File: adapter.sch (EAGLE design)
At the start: 3 parts

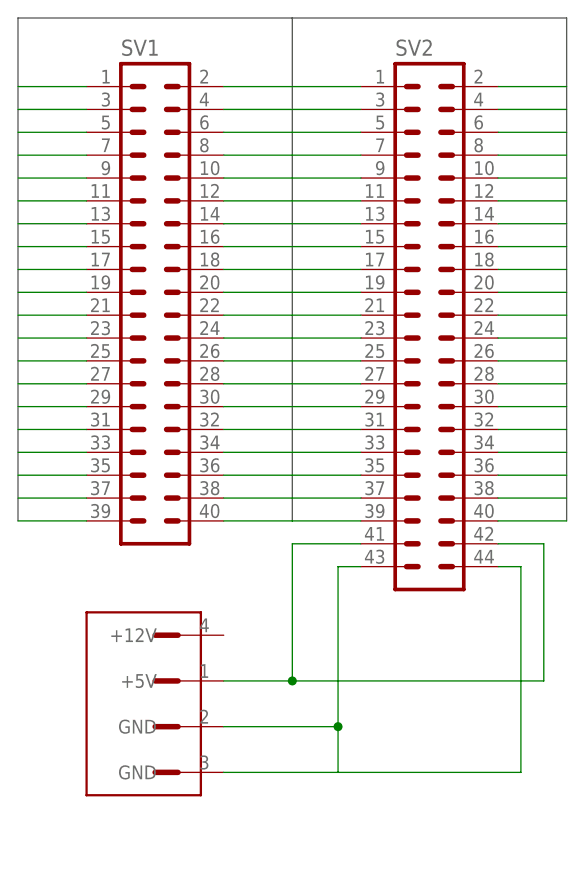
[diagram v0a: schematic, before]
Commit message: Connected the ground together.
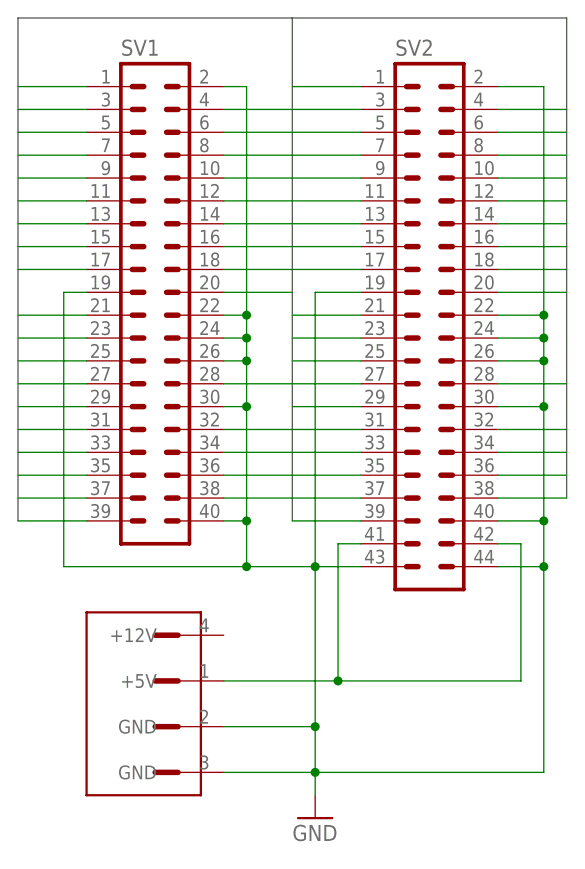
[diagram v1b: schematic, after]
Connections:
- removed net IDE19: SV1.GND@1, SV2.GND@1
- removed net IDE2: SV1.GND@2, SV2.GND@2
- removed net IDE22: SV1.GND@3, SV2.GND@3
- removed net IDE24: SV1.GND@4, SV2.GND@4
- removed net IDE26: SV1.GND@5, SV2.GND@5
- removed net IDE30: SV1.GND@6, SV2.GND@6
- removed net IDE40: SV1.GND@7, SV2.GND@7
- removed net N$1: SV2.!TYPE!, SV2.GND@8, U$1.GND@1, U$1.GND@2
- new net GND: SV1.GND@1, SV1.GND@2, SV1.GND@3, SV1.GND@4, SV1.GND@5, SV1.GND@6, SV1.GND@7, SV2.!TYPE!, SV2.GND@1, SV2.GND@2, SV2.GND@3, SV2.GND@4, SV2.GND@5, SV2.GND@6, SV2.GND@7, SV2.GND@8, U$1.GND@1, U$1.GND@2
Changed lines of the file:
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@@
 <part name="SV2" library="conn" deviceset="IDE44" device="F"/>
 <part name="U$1" library="conn" deviceset="FLOPPYPWR" device=""/>
+<part name="GND1" library="supply1" deviceset="GND" device=""/>
 </parts>
 <sheets>
@@
 <instance part="SV2" gate="1" x="71.12" y="35.56"/>
 <instance part="U$1" gate="G$1" x="40.64" y="-7.62"/>
+<instance part="GND1" gate="1" x="58.42" y="-20.32"/>
 </instances>
 <busses>
@@
 <wire x1="55.88" y1="12.7" x2="55.88" y2="68.58" width="0.762" layer="92"/>
 <wire x1="55.88" y1="68.58" x2="86.36" y2="68.58" width="0.762" layer="92"/>
-<wire x1="86.36" y1="68.58" x2="86.36" y2="12.7" width="0.762" layer="92"/>
+<wire x1="86.36" y1="68.58" x2="86.36" y2="15.24" width="0.762" layer="92"/>
 <wire x1="55.88" y1="68.58" x2="25.4" y2="68.58" width="0.762" layer="92"/>
 <wire x1="25.4" y1="68.58" x2="25.4" y2="12.7" width="0.762" layer="92"/>
@@
 </segment>
 </net>
-<net name="IDE19" class="0">
-<segment>
-<pinref part="SV1" gate="1" pin="GND@1"/>
-<wire x1="33.02" y1="38.1" x2="25.4" y2="38.1" width="0.1524" layer="91"/>
-</segment>
-<segment>
-<pinref part="SV2" gate="1" pin="GND@1"/>
-<wire x1="63.5" y1="38.1" x2="55.88" y2="38.1" width="0.1524" layer="91"/>
-</segment>
-</net>
 <net name="IDE21" class="0">
 <segment>
@@
 </segment>
 </net>
-<net name="IDE2" class="0">
-<segment>
+<net name="GND" class="0">
+<segment>
+<pinref part="U$1" gate="G$1" pin="GND@2"/>
+<wire x1="48.26" y1="-15.24" x2="58.42" y2="-15.24" width="0.1524" layer="91"/>
+<wire x1="58.42" y1="-15.24" x2="58.42" y2="-10.16" width="0.1524" layer="91"/>
+<pinref part="SV2" gate="1" pin="GND@8"/>
+<wire x1="58.42" y1="-10.16" x2="58.42" y2="7.62" width="0.1524" layer="91"/>
+<wire x1="58.42" y1="7.62" x2="63.5" y2="7.62" width="0.1524" layer="91"/>
+<pinref part="U$1" gate="G$1" pin="GND@1"/>
+<wire x1="48.26" y1="-10.16" x2="58.42" y2="-10.16" width="0.1524" layer="91"/>
+<junction x="58.42" y="-10.16"/>
+<pinref part="SV2" gate="1" pin="!TYPE!"/>
+<wire x1="78.74" y1="7.62" x2="83.82" y2="7.62" width="0.1524" layer="91"/>
+<wire x1="83.82" y1="7.62" x2="83.82" y2="-15.24" width="0.1524" layer="91"/>
+<wire x1="83.82" y1="-15.24" x2="58.42" y2="-15.24" width="0.1524" layer="91"/>
+<pinref part="GND1" gate="1" pin="GND"/>
+<wire x1="58.42" y1="-15.24" x2="58.42" y2="-17.78" width="0.1524" layer="91"/>
+<junction x="58.42" y="-15.24"/>
+<pinref part="SV2" gate="1" pin="GND@2"/>
+<wire x1="78.74" y1="60.96" x2="83.82" y2="60.96" width="0.1524" layer="91"/>
+<wire x1="83.82" y1="60.96" x2="83.82" y2="35.56" width="0.1524" layer="91"/>
+<pinref part="SV2" gate="1" pin="GND@5"/>
+<wire x1="83.82" y1="35.56" x2="83.82" y2="33.02" width="0.1524" layer="91"/>
+<wire x1="83.82" y1="33.02" x2="83.82" y2="30.48" width="0.1524" layer="91"/>
+<wire x1="83.82" y1="30.48" x2="83.82" y2="25.4" width="0.1524" layer="91"/>
+<wire x1="83.82" y1="25.4" x2="83.82" y2="12.7" width="0.1524" layer="91"/>
+<wire x1="83.82" y1="12.7" x2="83.82" y2="7.62" width="0.1524" layer="91"/>
+<wire x1="78.74" y1="30.48" x2="83.82" y2="30.48" width="0.1524" layer="91"/>
+<pinref part="SV2" gate="1" pin="GND@4"/>
+<wire x1="78.74" y1="33.02" x2="83.82" y2="33.02" width="0.1524" layer="91"/>
+<pinref part="SV2" gate="1" pin="GND@3"/>
+<wire x1="78.74" y1="35.56" x2="83.82" y2="35.56" width="0.1524" layer="91"/>
+<pinref part="SV2" gate="1" pin="GND@1"/>
+<wire x1="63.5" y1="38.1" x2="58.42" y2="38.1" width="0.1524" layer="91"/>
+<wire x1="58.42" y1="38.1" x2="58.42" y2="7.62" width="0.1524" layer="91"/>
+<junction x="58.42" y="7.62"/>
+<junction x="83.82" y="7.62"/>
+<junction x="83.82" y="30.48"/>
+<junction x="83.82" y="33.02"/>
+<junction x="83.82" y="35.56"/>
+<pinref part="SV2" gate="1" pin="GND@6"/>
+<wire x1="83.82" y1="25.4" x2="78.74" y2="25.4" width="0.1524" layer="91"/>
+<junction x="83.82" y="25.4"/>
+<pinref part="SV2" gate="1" pin="GND@7"/>
+<wire x1="78.74" y1="12.7" x2="83.82" y2="12.7" width="0.1524" layer="91"/>
+<junction x="83.82" y="12.7"/>
+<pinref part="SV1" gate="1" pin="GND@3"/>
+<wire x1="48.26" y1="35.56" x2="50.8" y2="35.56" width="0.1524" layer="91"/>
+<wire x1="50.8" y1="35.56" x2="50.8" y2="33.02" width="0.1524" layer="91"/>
+<wire x1="50.8" y1="33.02" x2="50.8" y2="30.48" width="0.1524" layer="91"/>
+<wire x1="50.8" y1="30.48" x2="50.8" y2="25.4" width="0.1524" layer="91"/>
+<wire x1="50.8" y1="25.4" x2="50.8" y2="12.7" width="0.1524" layer="91"/>
+<wire x1="50.8" y1="12.7" x2="50.8" y2="7.62" width="0.1524" layer="91"/>
+<wire x1="50.8" y1="7.62" x2="58.42" y2="7.62" width="0.1524" layer="91"/>
+<pinref part="SV1" gate="1" pin="GND@7"/>
+<wire x1="48.26" y1="12.7" x2="50.8" y2="12.7" width="0.1524" layer="91"/>
+<pinref part="SV1" gate="1" pin="GND@6"/>
+<wire x1="48.26" y1="25.4" x2="50.8" y2="25.4" width="0.1524" layer="91"/>
+<pinref part="SV1" gate="1" pin="GND@4"/>
+<wire x1="48.26" y1="33.02" x2="50.8" y2="33.02" width="0.1524" layer="91"/>
+<pinref part="SV1" gate="1" pin="GND@5"/>
+<wire x1="48.26" y1="30.48" x2="50.8" y2="30.48" width="0.1524" layer="91"/>
 <pinref part="SV1" gate="1" pin="GND@2"/>
-<wire x1="48.26" y1="60.96" x2="55.88" y2="60.96" width="0.1524" layer="91"/>
-</segment>
-<segment>
-<pinref part="SV2" gate="1" pin="GND@2"/>
-<wire x1="78.74" y1="60.96" x2="86.36" y2="60.96" width="0.1524" layer="91"/>
+<wire x1="48.26" y1="60.96" x2="50.8" y2="60.96" width="0.1524" layer="91"/>
+<wire x1="50.8" y1="60.96" x2="50.8" y2="35.56" width="0.1524" layer="91"/>
+<pinref part="SV1" gate="1" pin="GND@1"/>
+<wire x1="33.02" y1="38.1" x2="30.48" y2="38.1" width="0.1524" layer="91"/>
+<wire x1="30.48" y1="38.1" x2="30.48" y2="7.62" width="0.1524" layer="91"/>
+<wire x1="30.48" y1="7.62" x2="50.8" y2="7.62" width="0.1524" layer="91"/>
+<junction x="50.8" y="35.56"/>
+<junction x="50.8" y="33.02"/>
+<junction x="50.8" y="30.48"/>
+<junction x="50.8" y="25.4"/>
+<junction x="50.8" y="12.7"/>
+<junction x="50.8" y="7.62"/>
 </segment>
 </net>
@@
 </segment>
 </net>
-<net name="IDE22" class="0">
-<segment>
-<pinref part="SV1" gate="1" pin="GND@3"/>
-<wire x1="48.26" y1="35.56" x2="55.88" y2="35.56" width="0.1524" layer="91"/>
-</segment>
-<segment>
-<pinref part="SV2" gate="1" pin="GND@3"/>
-<wire x1="78.74" y1="35.56" x2="86.36" y2="35.56" width="0.1524" layer="91"/>
-</segment>
-</net>
-<net name="IDE24" class="0">
-<segment>
-<pinref part="SV1" gate="1" pin="GND@4"/>
-<wire x1="48.26" y1="33.02" x2="55.88" y2="33.02" width="0.1524" layer="91"/>
-</segment>
-<segment>
-<pinref part="SV2" gate="1" pin="GND@4"/>
-<wire x1="78.74" y1="33.02" x2="86.36" y2="33.02" width="0.1524" layer="91"/>
-</segment>
-</net>
-<net name="IDE26" class="0">
-<segment>
-<pinref part="SV1" gate="1" pin="GND@5"/>
-<wire x1="48.26" y1="30.48" x2="55.88" y2="30.48" width="0.1524" layer="91"/>
-</segment>
-<segment>
-<pinref part="SV2" gate="1" pin="GND@5"/>
-<wire x1="78.74" y1="30.48" x2="86.36" y2="30.48" width="0.1524" layer="91"/>
-</segment>
-</net>
 <net name="IDE28" class="0">
 <segment>
@@
 </segment>
 </net>
-<net name="IDE30" class="0">
-<segment>
-<pinref part="SV1" gate="1" pin="GND@6"/>
-<wire x1="48.26" y1="25.4" x2="55.88" y2="25.4" width="0.1524" layer="91"/>
-</segment>
-<segment>
-<pinref part="SV2" gate="1" pin="GND@6"/>
-<wire x1="78.74" y1="25.4" x2="86.36" y2="25.4" width="0.1524" layer="91"/>
-</segment>
-</net>
 <net name="IDE32" class="0">
 <segment>
@@
 </segment>
 </net>
-<net name="IDE40" class="0">
-<segment>
-<pinref part="SV1" gate="1" pin="GND@7"/>
-<wire x1="48.26" y1="12.7" x2="55.88" y2="12.7" width="0.1524" layer="91"/>
-</segment>
-<segment>
-<pinref part="SV2" gate="1" pin="GND@7"/>
-<wire x1="78.74" y1="12.7" x2="86.36" y2="12.7" width="0.1524" layer="91"/>
-</segment>
-</net>
-<net name="N$1" class="0">
-<segment>
-<pinref part="U$1" gate="G$1" pin="GND@2"/>
-<wire x1="48.26" y1="-15.24" x2="60.96" y2="-15.24" width="0.1524" layer="91"/>
-<wire x1="60.96" y1="-15.24" x2="60.96" y2="-10.16" width="0.1524" layer="91"/>
-<pinref part="SV2" gate="1" pin="GND@8"/>
-<wire x1="60.96" y1="-10.16" x2="60.96" y2="7.62" width="0.1524" layer="91"/>
-<wire x1="60.96" y1="7.62" x2="63.5" y2="7.62" width="0.1524" layer="91"/>
-<pinref part="U$1" gate="G$1" pin="GND@1"/>
-<wire x1="48.26" y1="-10.16" x2="60.96" y2="-10.16" width="0.1524" layer="91"/>
-<junction x="60.96" y="-10.16"/>
-<pinref part="SV2" gate="1" pin="!TYPE!"/>
-<wire x1="78.74" y1="7.62" x2="81.28" y2="7.62" width="0.1524" layer="91"/>
-<wire x1="81.28" y1="7.62" x2="81.28" y2="-15.24" width="0.1524" layer="91"/>
-<wire x1="81.28" y1="-15.24" x2="60.96" y2="-15.24" width="0.1524" layer="91"/>
-</segment>
-</net>
 <net name="N$3" class="0">
 <segment>
 <pinref part="U$1" gate="G$1" pin="+5V"/>
-<wire x1="48.26" y1="-5.08" x2="55.88" y2="-5.08" width="0.1524" layer="91"/>
-<wire x1="55.88" y1="-5.08" x2="55.88" y2="10.16" width="0.1524" layer="91"/>
+<wire x1="48.26" y1="-5.08" x2="60.96" y2="-5.08" width="0.1524" layer="91"/>
+<wire x1="60.96" y1="-5.08" x2="81.28" y2="-5.08" width="0.1524" layer="91"/>
+<wire x1="81.28" y1="-5.08" x2="81.28" y2="10.16" width="0.1524" layer="91"/>
+<pinref part="SV2" gate="1" pin="VCC@2"/>
+<wire x1="81.28" y1="10.16" x2="78.74" y2="10.16" width="0.1524" layer="91"/>
 <pinref part="SV2" gate="1" pin="VCC@1"/>
-<wire x1="55.88" y1="10.16" x2="63.5" y2="10.16" width="0.1524" layer="91"/>
-<wire x1="55.88" y1="-5.08" x2="83.82" y2="-5.08" width="0.1524" layer="91"/>
-<wire x1="83.82" y1="-5.08" x2="83.82" y2="10.16" width="0.1524" layer="91"/>
-<pinref part="SV2" gate="1" pin="VCC@2"/>
-<wire x1="83.82" y1="10.16" x2="78.74" y2="10.16" width="0.1524" layer="91"/>
-<junction x="55.88" y="-5.08"/>
-</segment>
-</net>
+<wire x1="63.5" y1="10.16" x2="60.96" y2="10.16" width="0.1524" layer="91"/>
+<wire x1="60.96" y1="10.16" x2="60.96" y2="-5.08" width="0.1524" layer="91"/>
+<junction x="60.96" y="-5.08"/>
+</segment>
+</net>

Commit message: Reduced pin pitch on the IDE 44 connector.
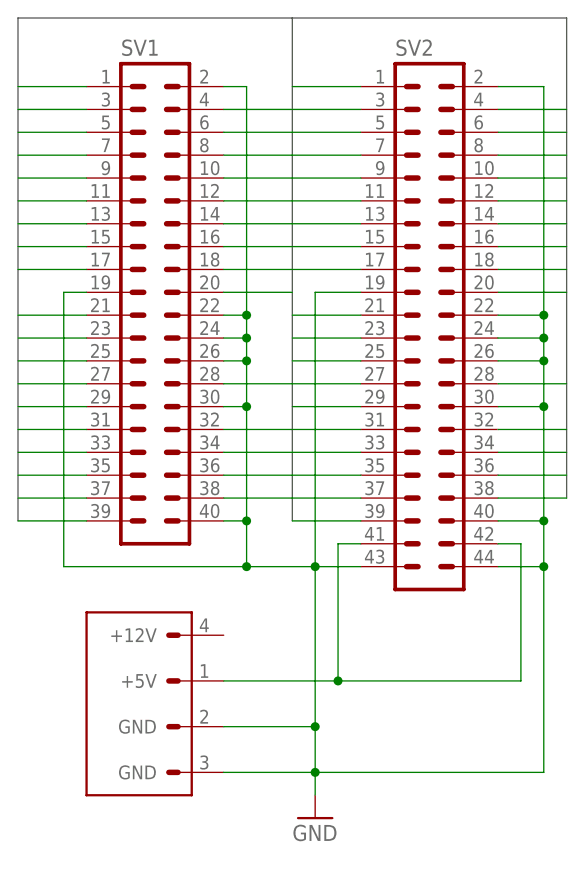
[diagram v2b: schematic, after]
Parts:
- SV2: device conn:IDE44F -> conn:IDE44LOWPITCHF
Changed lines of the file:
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@@
 <grid distance="0.1" unitdist="inch" unit="inch" style="lines" multiple="1" display="no" altdistance="0.01" altunitdist="inch" altunit="inch"/>
 <layers>
-<layer number="1" name="Top" color="4" fill="1" visible="no" active="no"/>
-<layer number="16" name="Bottom" color="1" fill="1" visible="no" active="no"/>
-<layer number="17" name="Pads" color="2" fill="1" visible="no" active="no"/>
-<layer number="18" name="Vias" color="2" fill="1" visible="no" active="no"/>
-<layer number="19" name="Unrouted" color="6" fill="1" visible="no" active="no"/>
-<layer number="20" name="Dimension" color="15" fill="1" visible="no" active="no"/>
-<layer number="21" name="tPlace" color="7" fill="1" visible="no" active="no"/>
-<layer number="22" name="bPlace" color="7" fill="1" visible="no" active="no"/>
-<layer number="23" name="tOrigins" color="15" fill="1" visible="no" active="no"/>
-<layer number="24" name="bOrigins" color="15" fill="1" visible="no" active="no"/>
-<layer number="25" name="tNames" color="7" fill="1" visible="no" active="no"/>
-<layer number="26" name="bNames" color="7" fill="1" visible="no" active="no"/>
-<layer number="27" name="tValues" color="7" fill="1" visible="no" active="no"/>
-<layer number="28" name="bValues" color="7" fill="1" visible="no" active="no"/>
+<layer number="1" name="Top" color="4" fill="1" visible="yes" active="no"/>
+<layer number="16" name="Bottom" color="1" fill="1" visible="yes" active="no"/>
+<layer number="17" name="Pads" color="2" fill="1" visible="yes" active="no"/>
+<layer number="18" name="Vias" color="2" fill="1" visible="yes" active="no"/>
+<layer number="19" name="Unrouted" color="6" fill="1" visible="yes" active="no"/>
+<layer number="20" name="Dimension" color="15" fill="1" visible="yes" active="no"/>
+<layer number="21" name="tPlace" color="7" fill="1" visible="yes" active="no"/>
+<layer number="22" name="bPlace" color="7" fill="1" visible="yes" active="no"/>
+<layer number="23" name="tOrigins" color="15" fill="1" visible="yes" active="no"/>
+<layer number="24" name="bOrigins" color="15" fill="1" visible="yes" active="no"/>
+<layer number="25" name="tNames" color="7" fill="1" visible="yes" active="no"/>
+<layer number="26" name="bNames" color="7" fill="1" visible="yes" active="no"/>
+<layer number="27" name="tValues" color="7" fill="1" visible="yes" active="no"/>
+<layer number="28" name="bValues" color="7" fill="1" visible="yes" active="no"/>
 <layer number="29" name="tStop" color="7" fill="3" visible="no" active="no"/>
 <layer number="30" name="bStop" color="7" fill="6" visible="no" active="no"/>
@@
 <layer number="35" name="tGlue" color="7" fill="4" visible="no" active="no"/>
 <layer number="36" name="bGlue" color="7" fill="5" visible="no" active="no"/>
-<layer number="37" name="tTest" color="7" fill="1" visible="no" active="no"/>
-<layer number="38" name="bTest" color="7" fill="1" visible="no" active="no"/>
+<layer number="37" name="tTest" color="7" fill="1" visible="yes" active="no"/>
+<layer number="38" name="bTest" color="7" fill="1" visible="yes" active="no"/>
 <layer number="39" name="tKeepout" color="4" fill="11" visible="no" active="no"/>
 <layer number="40" name="bKeepout" color="1" fill="11" visible="no" active="no"/>
@@
 <layer number="44" name="Drills" color="7" fill="1" visible="no" active="no"/>
 <layer number="45" name="Holes" color="7" fill="1" visible="no" active="no"/>
-<layer number="46" name="Milling" color="3" fill="1" visible="no" active="no"/>
-<layer number="47" name="Measures" color="7" fill="1" visible="no" active="no"/>
-<layer number="48" name="Document" color="7" fill="1" visible="no" active="no"/>
-<layer number="49" name="Reference" color="7" fill="1" visible="no" active="no"/>
-<layer number="51" name="tDocu" color="7" fill="1" visible="no" active="no"/>
-<layer number="52" name="bDocu" color="7" fill="1" visible="no" active="no"/>
+<layer number="46" name="Milling" color="3" fill="1" visible="yes" active="no"/>
+<layer number="47" name="Measures" color="7" fill="1" visible="yes" active="no"/>
+<layer number="48" name="Document" color="7" fill="1" visible="yes" active="no"/>
+<layer number="49" name="Reference" color="7" fill="1" visible="yes" active="no"/>
+<layer number="51" name="tDocu" color="7" fill="1" visible="yes" active="no"/>
+<layer number="52" name="bDocu" color="7" fill="1" visible="yes" active="no"/>
 <layer number="90" name="Modules" color="5" fill="1" visible="yes" active="yes"/>
 <layer number="91" name="Nets" color="2" fill="1" visible="yes" active="yes"/>
@@
 <parts>
 <part name="SV1" library="conn" deviceset="IDE40" device=""/>
-<part name="SV2" library="conn" deviceset="IDE44" device="F"/>
+<part name="SV2" library="conn" deviceset="IDE44" device="LOWPITCHF"/>
 <part name="U$1" library="conn" deviceset="FLOPPYPWR" device=""/>
 <part name="GND1" library="supply1" deviceset="GND" device=""/>
